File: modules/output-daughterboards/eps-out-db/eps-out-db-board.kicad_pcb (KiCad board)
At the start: 4 copper layers, 67.8 x 11 mm, 7 parts, among them J1 EPS8 OUT FIELD, J10 TE 63951-1, J11 TE 63951-1, J12 TE 63951-1, J13 TE 63951-1, J14 TE 63951-1, J15 TE 63951-1

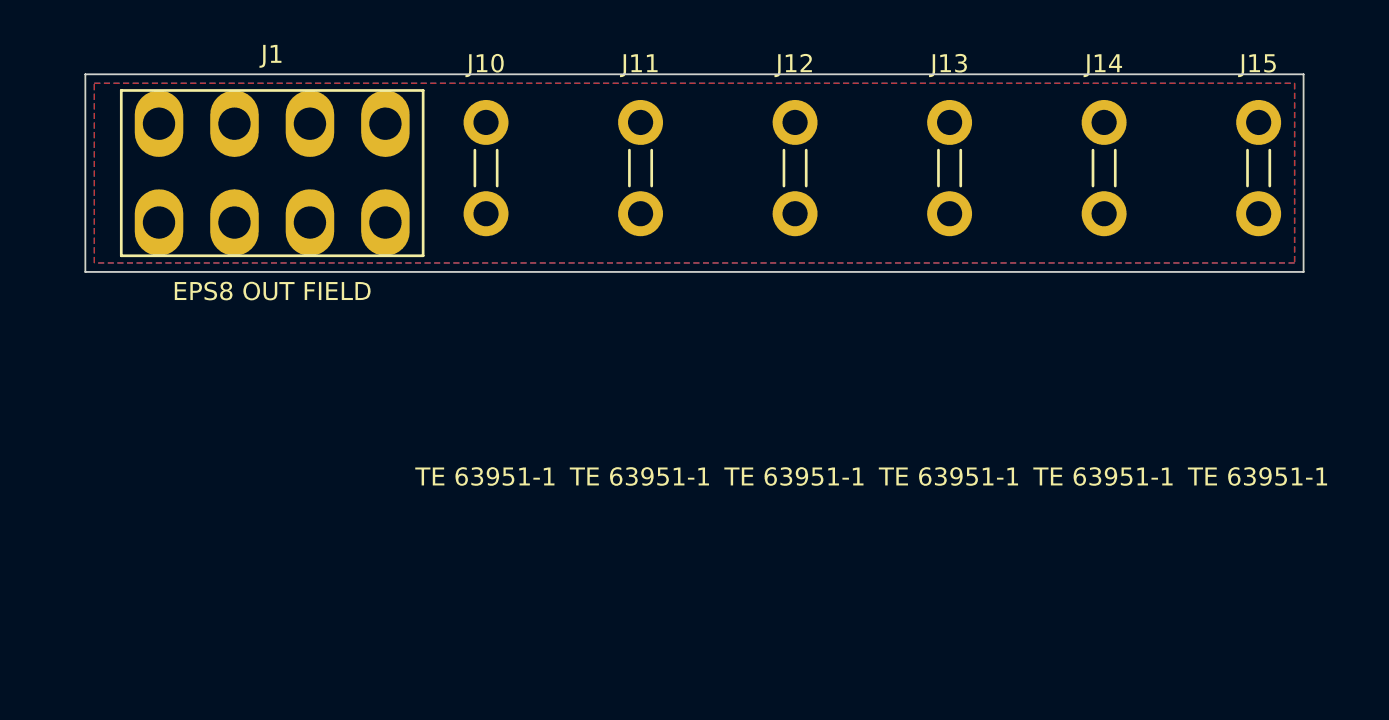
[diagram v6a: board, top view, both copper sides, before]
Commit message: Daughterboard iteration 4 LANDED: compact two-band — tabs packed below the pinout; honest heights 21.4/20.0/20.0mm
- Pitch floor derived: clip SMD pad span 6.60mm binding + 0.50 clearance = 7.10mm; chosen 7.1 (pcie, at floor) / 7.6 (eps, keying) / 8.4 (atx24, field-lattice-aligned so tab stubs clear field stubs by >=1.05mm)
- Keying: pitch differentiation alone survives the packed floor (no-subset margins >=1.5x the 0.5mm tolerance); teeth re-verified (sabotaged 7.2 eps pitch correctly fails)
- Seating invariant flipped to bottom-pinned: leg row 4.34mm above each bottom edge, float uniform 12.41mm at 1.0mm tip clearance
- Coordinator re-verified: ERC 0 x3, DRC 0/0 severity-error x3, checker fully green, identity 15/2/2 groups vs baseline
- owner-queue fit-check row dims updated (iteration-3 long-sliver variant retained in history)

Co-Authored-By: Claude Fable 5 <noreply@anthropic.com>
Claude-Session: https://claude.ai/code/session_01LvfqcnEeuin2oyJQw548EX
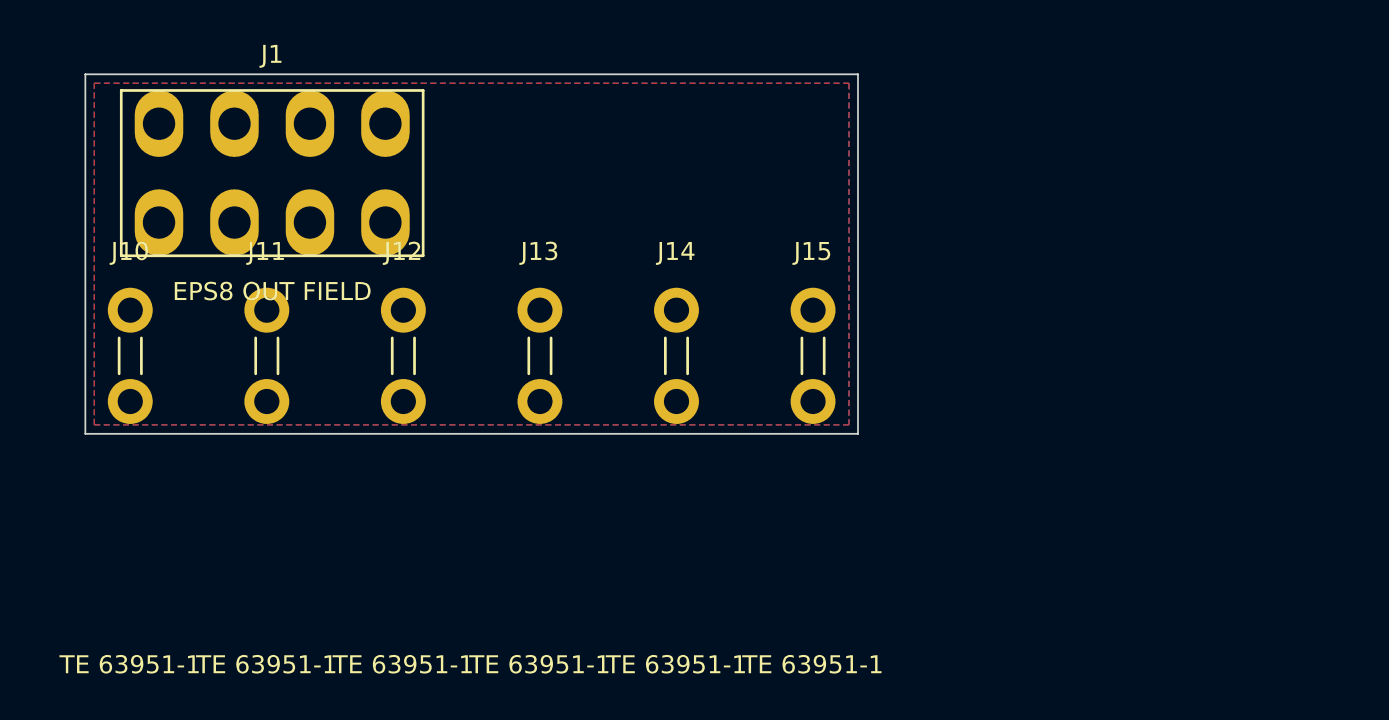
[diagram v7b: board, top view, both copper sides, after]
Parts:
- moved J15 26.9 mm to (40.5, 15.7)
- moved J14 26.0 mm to (32.9, 15.7)
- moved J13 25.1 mm to (25.3, 15.7)
- moved J12 24.2 mm to (17.7, 15.7)
- moved J11 23.3 mm to (10.1, 15.7)
- moved J10 22.4 mm to (2.50, 15.7)
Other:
- board size 67.8 x 11 mm -> 43 x 20 mm

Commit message: WIP snapshot: iteration-5 boards regenerating + checker update in flight (durability)
Co-Authored-By: Claude Fable 5 <noreply@anthropic.com>
Claude-Session: https://claude.ai/code/session_01LvfqcnEeuin2oyJQw548EX
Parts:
- moved J15 4.50 mm to (36.0, 15.7)
- moved J14 3.60 mm to (29.3, 15.7)
- moved J13 2.70 mm to (22.6, 15.7)
- moved J12 1.80 mm to (15.9, 15.7)
- moved J11 0.90 mm to (9.20, 15.7)
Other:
- board size 43 x 20 mm -> 38.5 x 20 mm
